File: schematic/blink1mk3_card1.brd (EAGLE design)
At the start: 88.5 x 50.8 mm, 37 parts, among them J1 NONPOP, U2 EFM32HG309F64G, X2 USBPCB2

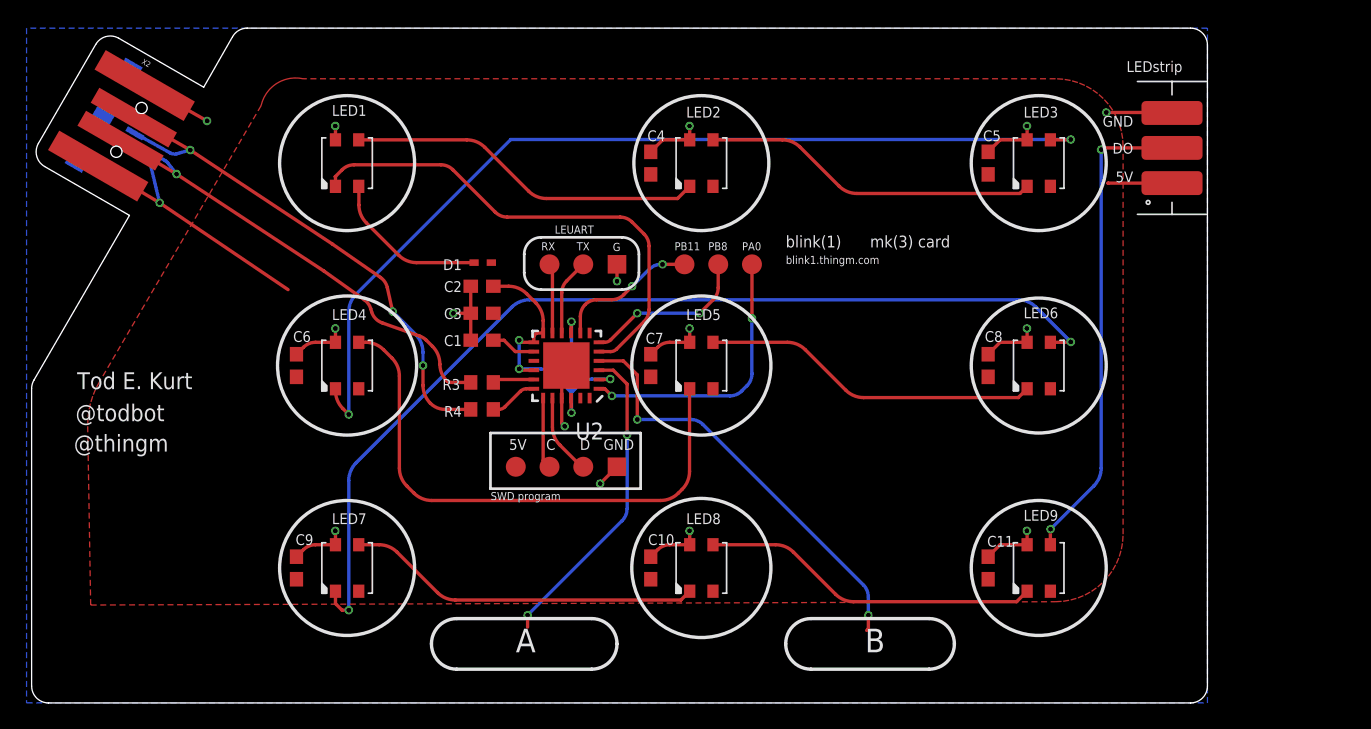
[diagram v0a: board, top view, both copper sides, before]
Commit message: fix EFM32HG309 pad spacing issue. omg what a slog
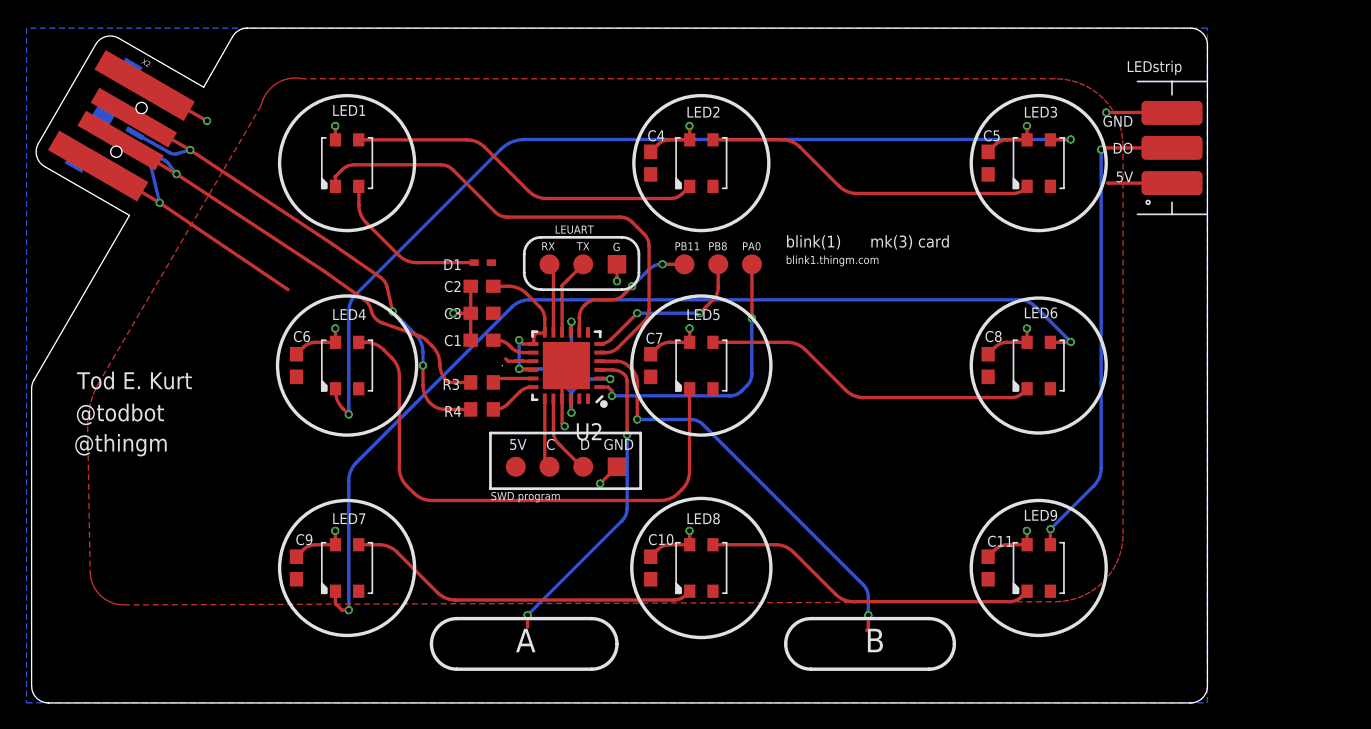
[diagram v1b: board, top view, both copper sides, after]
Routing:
- net +5V: track 27.1 -> 29.2 mm

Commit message: fix QFN footprint again, add blink1mk3_card2
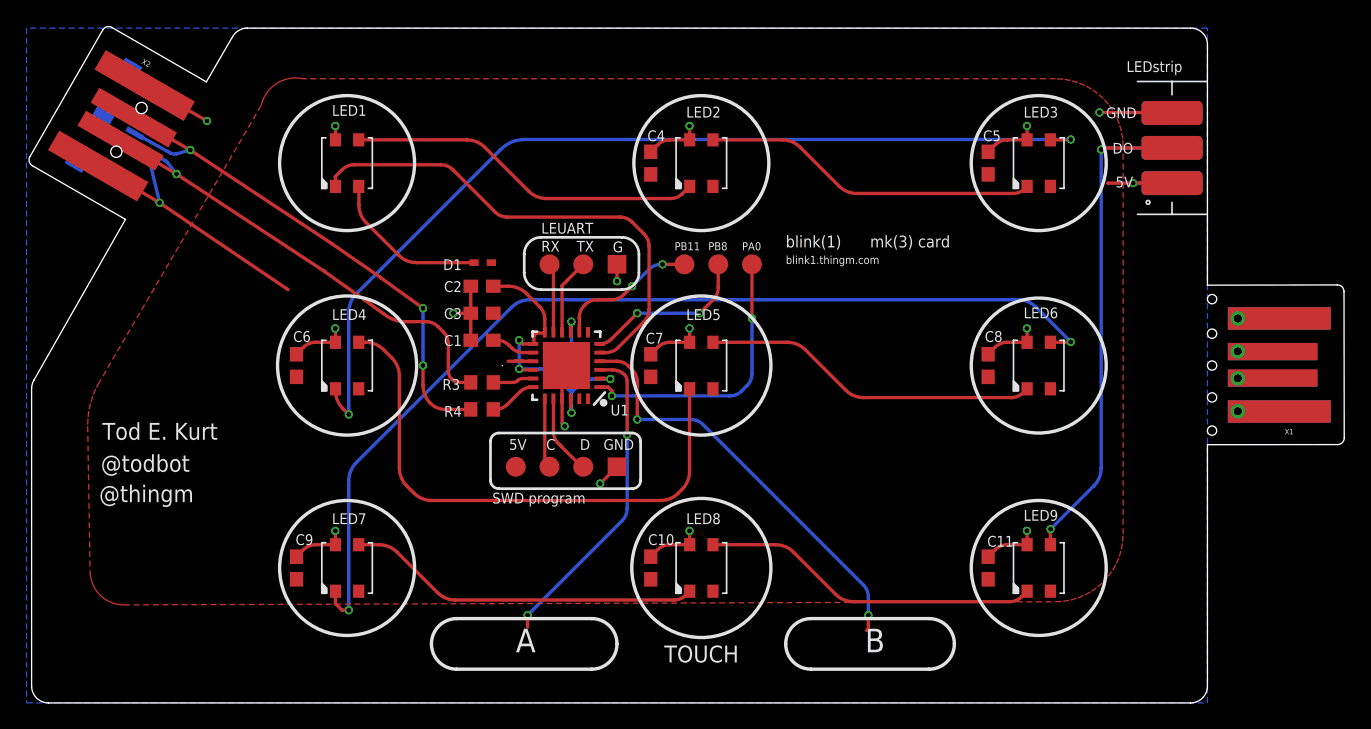
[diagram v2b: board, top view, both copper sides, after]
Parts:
- added U$2: LED_STRIP_3P, NeoJoints:LEDSTRIP-3P
- added X1: USBPCB2SIDE, todstuff:USB-A-PCB-TWOSIDED
- renumbered U2 to U1
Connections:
- new net VBUS: X1.5V@1, X1.5V@2, X1.5V@3
- net +5V: now also U$2.A
- net DO: now also U$2.B
- net GND: now also U$2.C, X1.GND@1, X1.GND@2, X1.GND@3
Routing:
- net DO: track 36.6 -> 42.0 mm
- net +5V: track 29.2 -> 31.9 mm, vias 1 -> 2
- net USB_D-: track 37.3 -> 38.0 mm
- net USB_D+: track 40.5 -> 41.1 mm
- net GND: track 58.9 -> 59.4 mm
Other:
- board size 88.5 x 50.8 mm -> 99 x 50.9 mm
- board text added: "TOUCH"
- board text added: "blink1mk3_card1"
- board text removed: "blink1mk3_card"
